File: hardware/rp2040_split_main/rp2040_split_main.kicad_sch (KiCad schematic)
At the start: 62 parts, among them J1 Conn_01x03, J2 Conn_01x03, J3 Conn_01x02, SW1 Reset, SW2 Boot, U1 RP2040, U2 IS31FL3743A-QULS4-TR, U3 W25Q32JVSS, U4 NCP1117-ADJ_SOT223, U5 PRTR5V0U2X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

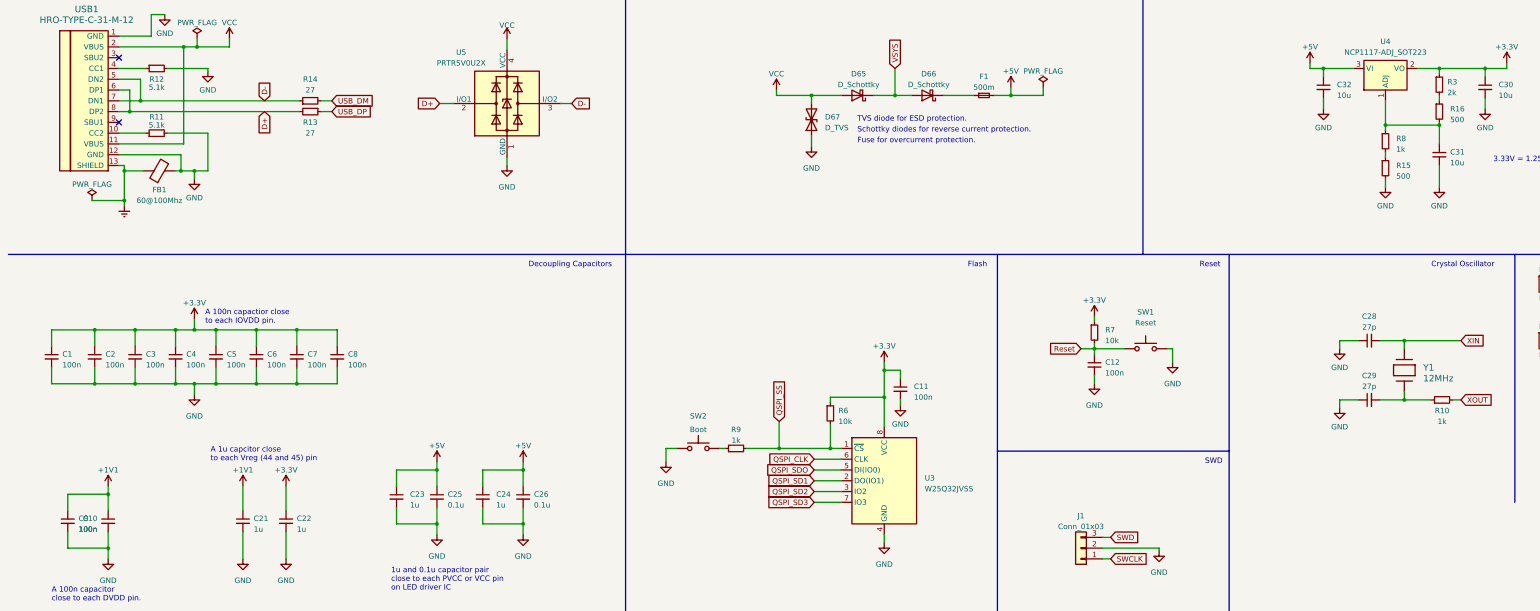
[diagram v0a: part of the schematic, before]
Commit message: Fixed Vreg circuit and silkscreen
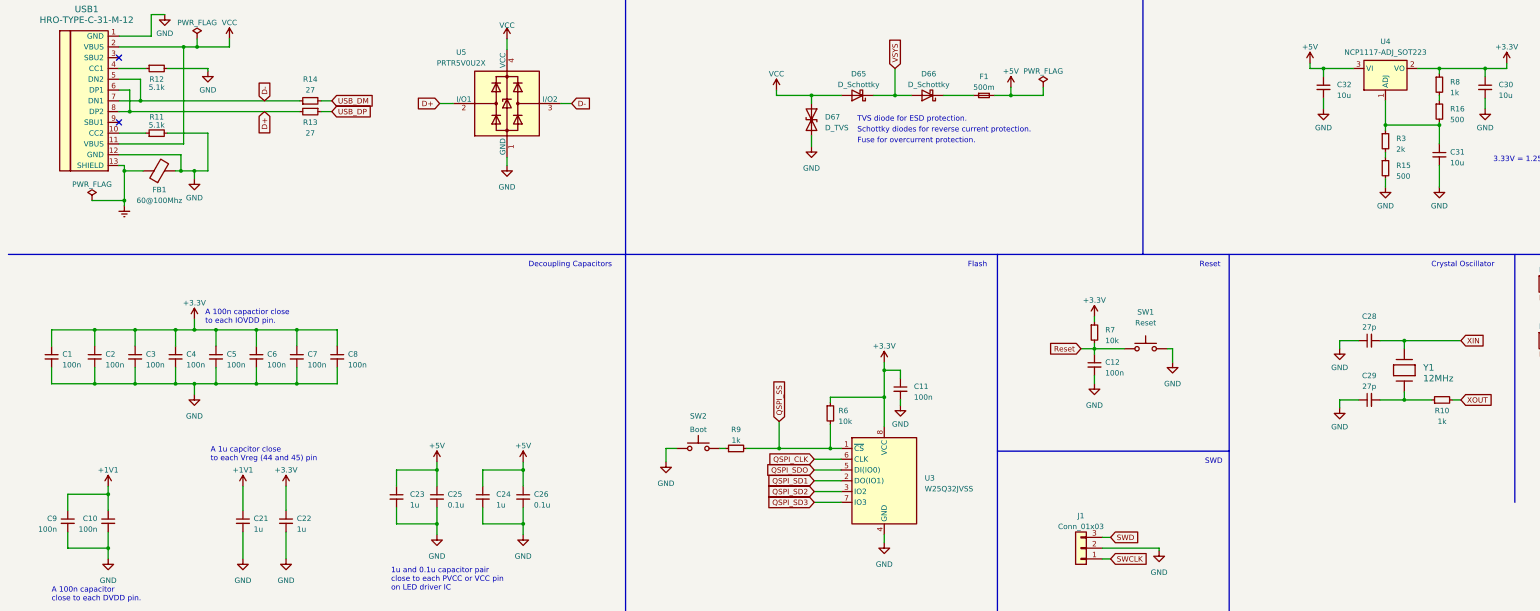
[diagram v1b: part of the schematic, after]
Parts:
- R3: renamed from R8; value 1k -> 2k
- R8: renamed from R3; value 2k -> 1k
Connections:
- net GND: now also D67.2 (A2); no longer D67.1 (A1)
- net VCC: now also D67.1 (A1); no longer D67.2 (A2)
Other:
- moved on the sheet: D67
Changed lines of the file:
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@@
     )
   )
-  (symbol (lib_id "Device:C_Small") (at 26.035 257.81 0) (unit 1)
-    (in_bom yes) (on_board yes) (dnp no) (fields_autoplaced)
-    (property "Reference" "C9" (at 28.575 257.1813 0)
-      (effects (font (size 1.27 1.27)) (justify left))
-    )
-    (property "Value" "100n" (at 28.575 259.7213 0)
+  (symbol (lib_id "Device:C_Small") (at 26.035 257.81 0) (mirror y) (unit 1)
+    (in_bom yes) (on_board yes) (dnp no)
+    (property "Reference" "C9" (at 23.495 257.1813 0)
+      (effects (font (size 1.27 1.27)) (justify left))
+    )
+    (property "Value" "100n" (at 23.495 259.7213 0)
       (effects (font (size 1.27 1.27)) (justify left))
     )
@@
   (symbol (lib_id "Device:R_Small") (at 349.25 154.94 0) (unit 1)
     (in_bom yes) (on_board yes) (dnp no) (fields_autoplaced)
-    (property "Reference" "R3" (at 351.155 154.305 0)
-      (effects (font (size 1.27 1.27)) (justify left))
-    )
-    (property "Value" "2k" (at 351.155 156.845 0)
+    (property "Reference" "R8" (at 351.79 154.305 0)
+      (effects (font (size 1.27 1.27)) (justify left))
+    )
+    (property "Value" "1k" (at 351.79 156.845 0)
       (effects (font (size 1.27 1.27)) (justify left))
     )
@@
       (project "rp2040_split_main"
         (path "/2d5068be-1ec7-4e39-96cf-6d6c4490ca13"
-          (reference "R3") (unit 1)
+          (reference "R8") (unit 1)
         )
       )
@@
   (symbol (lib_id "Device:R_Small") (at 336.55 168.275 0) (unit 1)
     (in_bom yes) (on_board yes) (dnp no) (fields_autoplaced)
-    (property "Reference" "R8" (at 339.09 167.64 0)
-      (effects (font (size 1.27 1.27)) (justify left))
-    )
-    (property "Value" "1k" (at 339.09 170.18 0)
+    (property "Reference" "R3" (at 339.09 167.64 0)
+      (effects (font (size 1.27 1.27)) (justify left))
+    )
+    (property "Value" "2k" (at 339.09 170.18 0)
       (effects (font (size 1.27 1.27)) (justify left))
     )
@@
       (project "rp2040_split_main"
         (path "/2d5068be-1ec7-4e39-96cf-6d6c4490ca13"
-          (reference "R8") (unit 1)
+          (reference "R3") (unit 1)
         )
       )
@@
     )
   )
-  (symbol (lib_id "Device:D_TVS") (at 201.295 163.195 90) (unit 1)
+  (symbol (lib_id "Device:D_TVS") (at 201.295 163.195 270) (unit 1)
     (in_bom yes) (on_board yes) (dnp no) (fields_autoplaced)
     (property "Reference" "D67" (at 204.47 162.56 90)
-      (effects (font (size 1.27 1.27)) (justify right))
+      (effects (font (size 1.27 1.27)) (justify left))
     )
     (property "Value" "D_TVS" (at 204.47 165.1 90)
-      (effects (font (size 1.27 1.27)) (justify right))
+      (effects (font (size 1.27 1.27)) (justify left))
     )
     (property "Footprint" "Diode_SMD:D_SOD-123" (at 201.295 163.195 0)
